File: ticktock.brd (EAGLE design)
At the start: 61 x 67.3 mm, 64 parts, among them IC1 ATMEGA644A, IC2 AD8611RM, IC3 REF200U, J1 AVR_SPI_PRG_6NS, Q1 MOSFET-NCHANNEL2N7002PW, Q2 MOSFET-NCHANNELBSS138, Q3 MOSFET-NCHANNELBSS138, U1 MAX232SOIC16, U2 OSCILLATORSMD, U3 FT232RLSSOP, U4 BMP180, X1 RS232

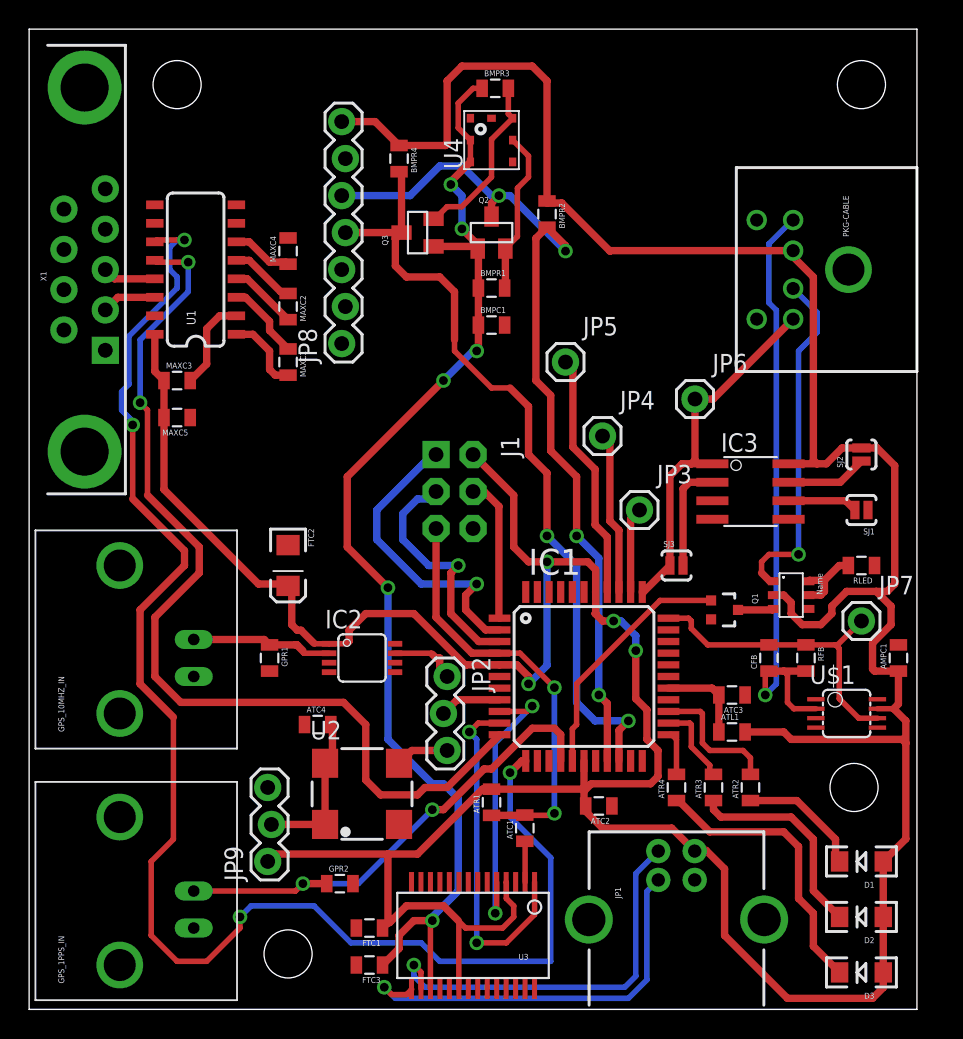
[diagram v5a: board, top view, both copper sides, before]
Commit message: add bottom ground plane
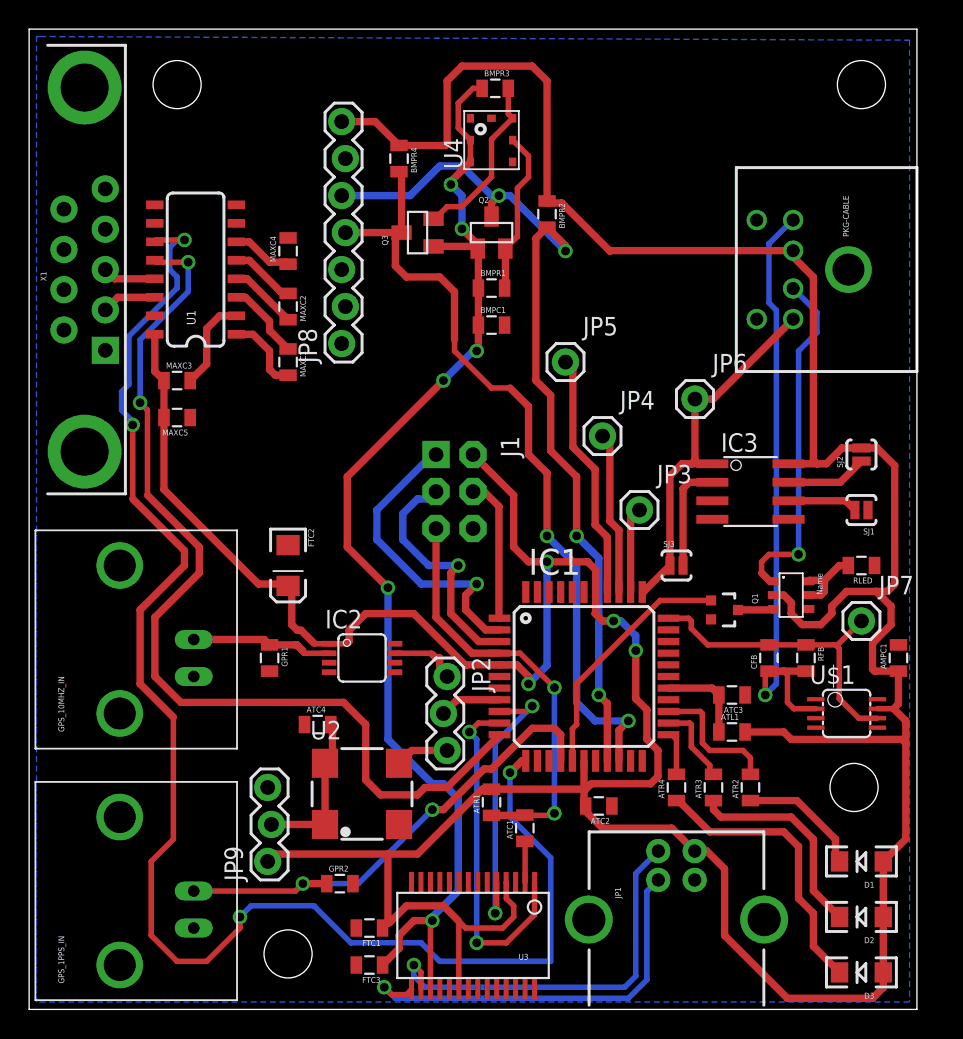
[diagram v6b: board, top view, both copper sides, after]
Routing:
- added copper zone on layer 16, net GND
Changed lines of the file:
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@@
 <?xml version="1.0" encoding="utf-8"?>
 <!DOCTYPE eagle SYSTEM "eagle.dtd">
-<eagle version="6.4">
+<eagle version="6.5.0">
 <drawing>
 <settings>
@@
 <grid distance="0.01" unitdist="inch" unit="inch" style="lines" multiple="1" display="yes" altdistance="0.02" altunitdist="inch" altunit="inch"/>
 <layers>
-<layer number="1" name="Top" color="4" fill="1" visible="yes" active="yes"/>
+<layer number="1" name="Top" color="4" fill="1" visible="no" active="yes"/>
 <layer number="16" name="Bottom" color="1" fill="1" visible="yes" active="yes"/>
 <layer number="17" name="Pads" color="2" fill="1" visible="yes" active="yes"/>
@@
 <layer number="42" name="bRestrict" color="1" fill="10" visible="no" active="yes"/>
 <layer number="43" name="vRestrict" color="2" fill="10" visible="no" active="yes"/>
-<layer number="44" name="Drills" color="7" fill="1" visible="yes" active="yes"/>
+<layer number="44" name="Drills" color="7" fill="1" visible="no" active="yes"/>
 <layer number="45" name="Holes" color="7" fill="1" visible="yes" active="yes"/>
 <layer number="46" name="Milling" color="3" fill="1" visible="yes" active="yes"/>
@@
 </elements>
 <signals>
-<signal name="GND" airwireshidden="yes">
+<signal name="GND">
 <contactref element="Q1" pad="2"/>
 <contactref element="AL5802" pad="GND"/>
@@
 <contactref element="U$1" pad="3"/>
 <contactref element="U$1" pad="4"/>
-<wire x1="49.96" y1="47.4" x2="49.96" y2="54.2" width="0" layer="19" extent="1-1"/>
-<wire x1="57.6" y1="34.29" x2="49.96" y2="47.4" width="0" layer="19" extent="1-1"/>
-<wire x1="58.05" y1="30.48" x2="57.6" y2="34.29" width="0" layer="19" extent="1-1"/>
-<wire x1="53.524" y1="27.498" x2="58.05" y2="30.48" width="0" layer="19" extent="1-1"/>
-<wire x1="59.69" y1="25.03" x2="58.05" y2="30.48" width="0" layer="19" extent="1-1"/>
-<wire x1="46.827" y1="26.782" x2="53.524" y2="27.498" width="0" layer="19" extent="1-1"/>
-<wire x1="43.9" y1="22.86" x2="46.827" y2="26.782" width="0" layer="19" extent="1-1"/>
+<polygon width="0.254" layer="16" isolate="0.6096">
+<vertex x="0.762" y="66.802"/>
+<vertex x="60.452" y="66.548"/>
+<vertex x="60.452" y="0.508"/>
+<vertex x="0.508" y="0.508"/>
+<vertex x="0.508" y="66.802"/>
+</polygon>
+<wire x1="32.65" y1="46.99" x2="31.75" y2="61.19" width="0" layer="19" extent="1-1"/>
+<wire x1="21.463" y1="45.72" x2="32.65" y2="46.99" width="0" layer="19" extent="1-1"/>
+<wire x1="16.51" y1="23.23" x2="11.303" y2="22.86" width="0" layer="19" extent="1-1"/>
+<wire x1="20.597" y1="23.156" x2="16.51" y2="23.23" width="0" layer="19" extent="1-1"/>
+<wire x1="20.597" y1="23.806" x2="20.597" y2="23.156" width="0" layer="19" extent="1-1"/>
+<wire x1="18.912" y1="19.558" x2="20.597" y2="23.156" width="0" layer="19" extent="1-1"/>
+<wire x1="25.122" y1="23.806" x2="20.597" y2="23.806" width="0" layer="19" extent="1-1"/>
+<wire x1="25.122" y1="23.156" x2="25.122" y2="23.806" width="0" layer="19" extent="1-1"/>
+<wire x1="32.3" y1="22.86" x2="25.122" y2="23.156" width="0" layer="19" extent="1-1"/>
+<wire x1="40.016" y1="13.97" x2="45.7" y2="8.89" width="0" layer="19" extent="1-1"/>
+<wire x1="38.9" y1="17.06" x2="40.016" y2="13.97" width="0" layer="19" extent="1-1"/>
+<wire x1="43.9" y1="22.86" x2="38.9" y2="17.06" width="0" layer="19" extent="1-1"/>
+<wire x1="46.827" y1="26.782" x2="43.9" y2="22.86" width="0" layer="19" extent="1-1"/>
 <wire x1="49.16" y1="21.59" x2="43.9" y2="22.86" width="0" layer="19" extent="1-1"/>
 <wire x1="54.021" y1="19.996" x2="49.16" y2="21.59" width="0" layer="19" extent="1-1"/>
 <wire x1="54.021" y1="19.346" x2="54.021" y2="19.996" width="0" layer="19" extent="1-1"/>
-<wire x1="38.9" y1="17.06" x2="43.9" y2="22.86" width="0" layer="19" extent="1-1"/>
-<wire x1="40.016" y1="13.97" x2="38.9" y2="17.06" width="0" layer="19" extent="1-1"/>
-<wire x1="45.7" y1="8.89" x2="40.016" y2="13.97" width="0" layer="19" extent="1-1"/>
-<wire x1="38.1" y1="28.66" x2="43.9" y2="22.86" width="0" layer="19" extent="1-1"/>
-<wire x1="32.3" y1="22.86" x2="38.1" y2="28.66" width="0" layer="19" extent="1-1"/>
-<wire x1="25.122" y1="23.156" x2="32.3" y2="22.86" width="0" layer="19" extent="1-1"/>
-<wire x1="25.122" y1="23.806" x2="25.122" y2="23.156" width="0" layer="19" extent="1-1"/>
-<wire x1="20.597" y1="23.806" x2="25.122" y2="23.806" width="0" layer="19" extent="1-1"/>
-<wire x1="20.597" y1="23.156" x2="20.597" y2="23.806" width="0" layer="19" extent="1-1"/>
-<wire x1="18.912" y1="19.558" x2="20.597" y2="23.156" width="0" layer="19" extent="1-1"/>
-<wire x1="16.51" y1="23.23" x2="20.597" y2="23.156" width="0" layer="19" extent="1-1"/>
-<wire x1="11.303" y1="22.86" x2="16.51" y2="23.23" width="0" layer="19" extent="1-1"/>
+<wire x1="53.524" y1="27.498" x2="46.827" y2="26.782" width="0" layer="19" extent="1-1"/>
+<wire x1="58.05" y1="30.48" x2="53.524" y2="27.498" width="0" layer="19" extent="1-1"/>
+<wire x1="57.6" y1="34.29" x2="58.05" y2="30.48" width="0" layer="19" extent="1-1"/>
+<wire x1="59.69" y1="25.03" x2="58.05" y2="30.48" width="0" layer="19" extent="1-1"/>
+<wire x1="17.78" y1="52.97" x2="21.463" y2="45.72" width="0" layer="19" extent="1-1"/>
+<wire x1="38.1" y1="28.66" x2="32.3" y2="22.86" width="0" layer="19" extent="1-1"/>
 <wire x1="17.78" y1="31.88" x2="20.597" y2="23.806" width="0" layer="19" extent="1-1"/>
-<wire x1="30.48" y1="33.02" x2="38.1" y2="28.66" width="0" layer="19" extent="1-1"/>
+<wire x1="8.63" y1="47.625" x2="5.23" y2="56.34" width="0" layer="19" extent="1-1"/>
+<wire x1="11.06" y1="40.64" x2="8.63" y2="47.625" width="0" layer="19" extent="1-1"/>
 <wire x1="25.4" y1="12.7" x2="18.912" y2="19.558" width="0" layer="19" extent="1-1"/>
 <wire x1="22.236" y1="8.636" x2="25.4" y2="12.7" width="0" layer="19" extent="1-1"/>
@@
 <wire x1="33.405" y1="1.424" x2="32.755" y2="1.424" width="0" layer="19" extent="1-1"/>
 <wire x1="30.805" y1="8.736" x2="25.4" y2="12.7" width="0" layer="19" extent="1-1"/>
-<wire x1="11.06" y1="40.64" x2="17.78" y2="31.88" width="0" layer="19" extent="1-1"/>
-<wire x1="8.63" y1="47.625" x2="11.06" y2="40.64" width="0" layer="19" extent="1-1"/>
-<wire x1="5.23" y1="56.34" x2="8.63" y2="47.625" width="0" layer="19" extent="1-1"/>
-<wire x1="17.78" y1="52.97" x2="8.63" y2="47.625" width="0" layer="19" extent="1-1"/>
-<wire x1="21.463" y1="45.72" x2="17.78" y2="52.97" width="0" layer="19" extent="1-1"/>
-<wire x1="11.303" y1="5.588" x2="22.468" y2="5.588" width="0" layer="19" extent="1-1"/>
-<wire x1="32.65" y1="46.99" x2="21.463" y2="45.72" width="0" layer="19" extent="1-1"/>
-<wire x1="31.75" y1="61.19" x2="32.65" y2="46.99" width="0" layer="19" extent="1-1"/>
 </signal>
 <signal name="IR_PWM">

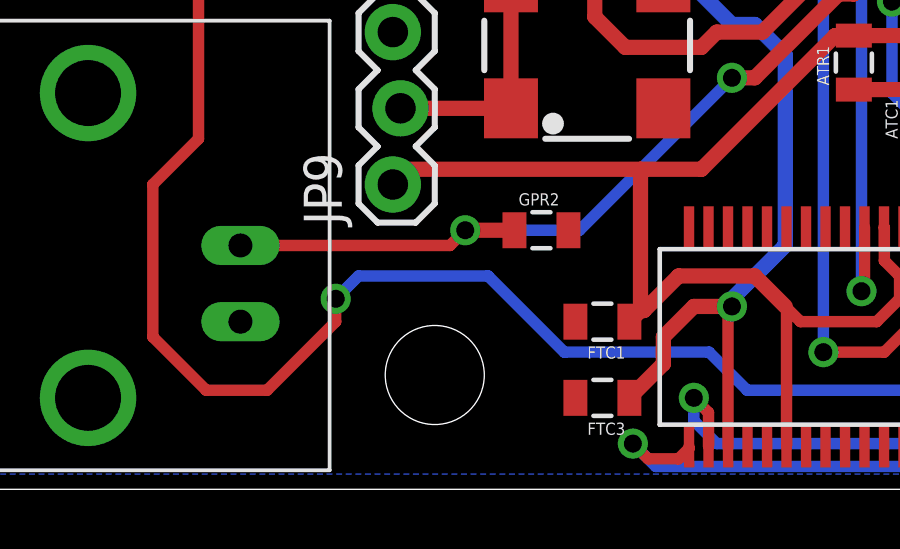
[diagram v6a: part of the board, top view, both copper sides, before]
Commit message: ease ground plane into a tight spot
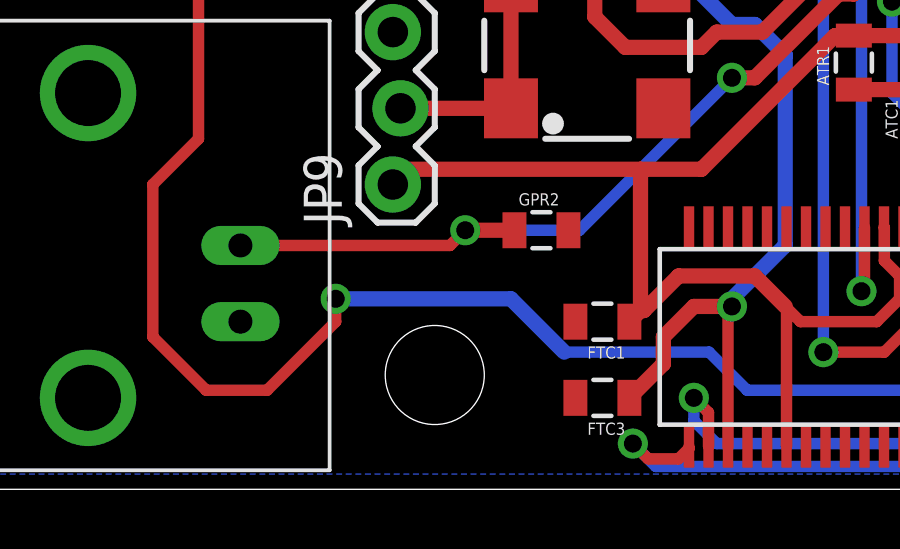
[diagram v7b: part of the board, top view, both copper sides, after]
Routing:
- net GPS_TX: track 104.3 -> 103.6 mm
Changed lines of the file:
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@@
 <grid distance="0.01" unitdist="inch" unit="inch" style="lines" multiple="1" display="yes" altdistance="0.02" altunitdist="inch" altunit="inch"/>
 <layers>
-<layer number="1" name="Top" color="4" fill="1" visible="no" active="yes"/>
+<layer number="1" name="Top" color="4" fill="1" visible="yes" active="yes"/>
 <layer number="16" name="Bottom" color="1" fill="1" visible="yes" active="yes"/>
 <layer number="17" name="Pads" color="2" fill="1" visible="yes" active="yes"/>
@@
 <layer number="37" name="tTest" color="7" fill="1" visible="yes" active="yes"/>
 <layer number="38" name="bTest" color="7" fill="1" visible="yes" active="yes"/>
-<layer number="39" name="tKeepout" color="4" fill="11" visible="no" active="yes"/>
-<layer number="40" name="bKeepout" color="1" fill="11" visible="no" active="yes"/>
+<layer number="39" name="tKeepout" color="4" fill="11" visible="yes" active="yes"/>
+<layer number="40" name="bKeepout" color="1" fill="11" visible="yes" active="yes"/>
 <layer number="41" name="tRestrict" color="4" fill="10" visible="no" active="yes"/>
 <layer number="42" name="bRestrict" color="1" fill="10" visible="no" active="yes"/>
@@
 <wire x1="28.194" y1="3.302" x2="26.924" y2="4.572" width="0.381" layer="16"/>
 <wire x1="26.924" y1="4.572" x2="22.098" y2="4.572" width="0.381" layer="16"/>
-<wire x1="22.098" y1="4.572" x2="19.558" y2="7.112" width="0.381" layer="16"/>
-<wire x1="19.558" y1="7.112" x2="15.24" y2="7.112" width="0.381" layer="16"/>
-<wire x1="15.24" y1="7.112" x2="14.478" y2="6.35" width="0.381" layer="16"/>
 <via x="14.478" y="6.35" extent="1-16" drill="0.6"/>
 <wire x1="14.478" y1="6.35" x2="14.478" y2="5.588" width="0.381" layer="1"/>
@@
 <wire x1="10.668" y1="52.832" x2="8.757" y2="52.832" width="0.381" layer="1"/>
 <wire x1="8.757" y1="52.832" x2="8.63" y2="52.705" width="0.381" layer="1"/>
+<wire x1="22.098" y1="4.572" x2="20.32" y2="6.35" width="0.508" layer="16"/>
+<wire x1="20.32" y1="6.35" x2="14.478" y2="6.35" width="0.508" layer="16"/>
 </signal>
 <signal name="N$8">
